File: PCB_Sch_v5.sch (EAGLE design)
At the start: 51 parts, among them IC1 CP2104, M1 C0720B001F, Q1 MMBT2222LT1G, Q2 mmbt2222, Q3 DMG3415U, Q4 mmbt2222, SW1 2-1825027-0, SW2 2-1825027-0, SW3 2-1825027-0, SW4 2-1825027-0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

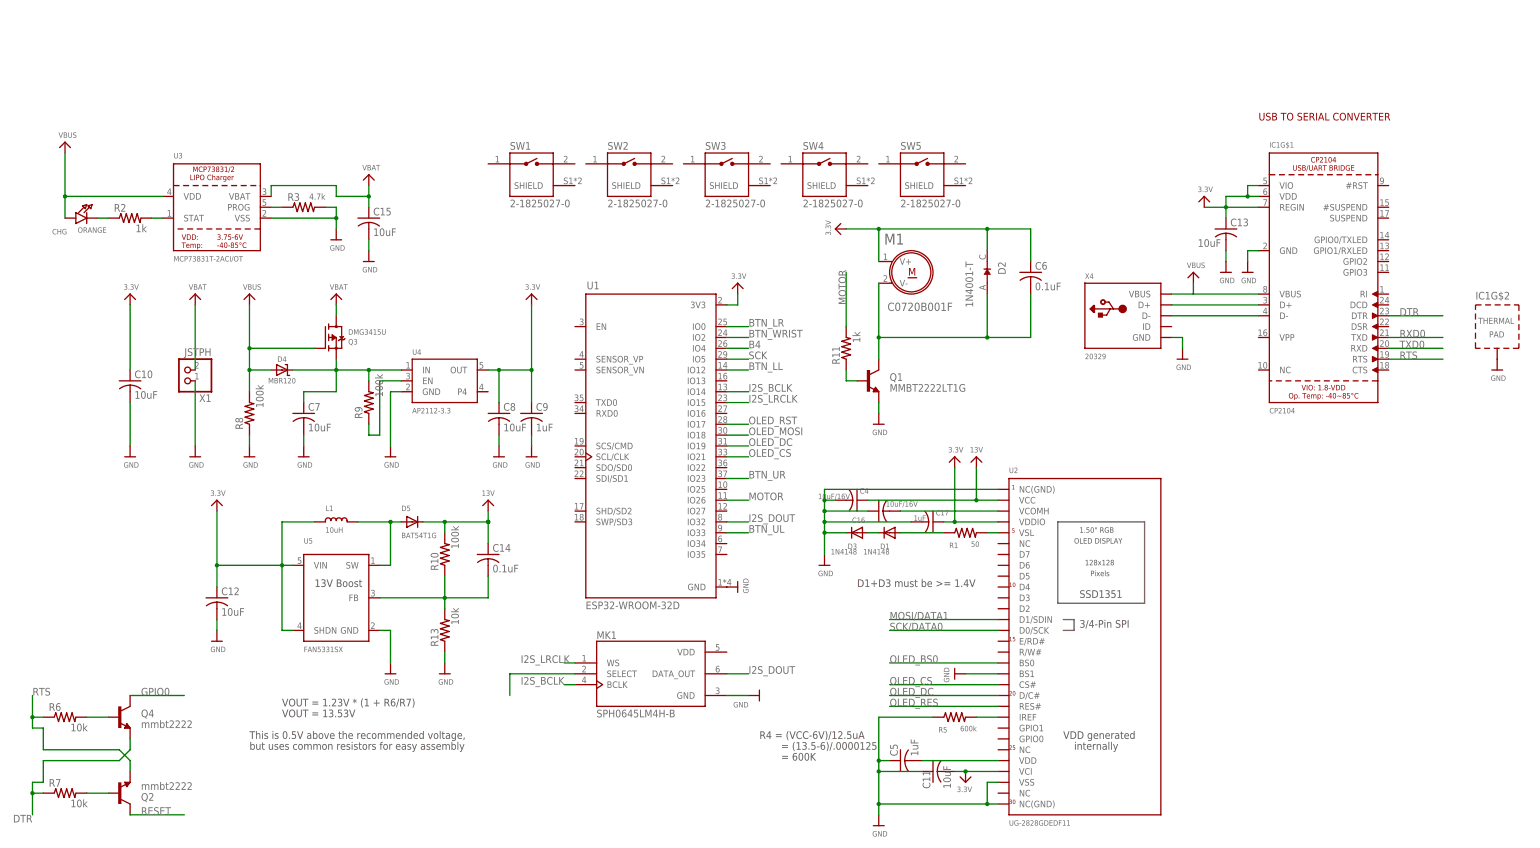
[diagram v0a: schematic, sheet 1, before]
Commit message: Added button to libraries, added debouncing caps
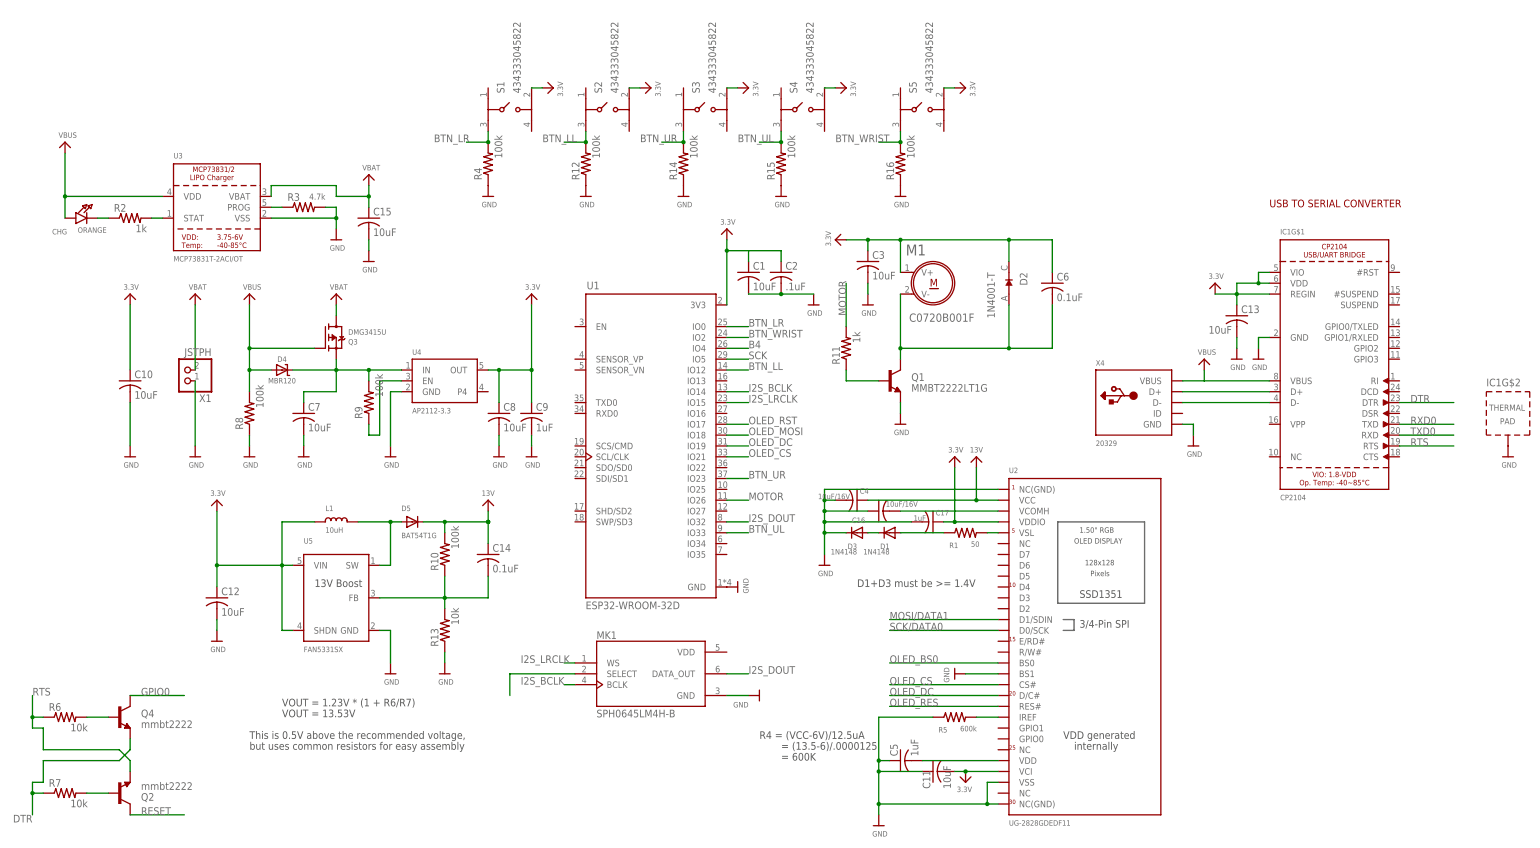
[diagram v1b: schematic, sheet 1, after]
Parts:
- removed SW1, SW2, SW3, SW4, SW5: 2-1825027-0, 2-1825027-0:2-1825027-0
- added C1, C3: 10uF, rcl:C-USC0603
- added C2: .1uF, rcl:C-USC0603
- added R12, R14, R15, R16, R4: 100k, rcl:R-US_R0603
- added S1, S2, S3, S4, S5: 434333045822, 434333045822:434333045822
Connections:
- net 3.3V: now also C1.1, C2.1, C3.1, S1.4, S2.4, S3.4, S4.4, S5.4
- net BTN_LL: now also R12.2, S2.1
- net BTN_LR: now also R4.2, S1.1
- net BTN_UL: now also R15.2, S4.1
- net BTN_UR: now also R14.2, S3.1
- net BTN_WRIST: now also R16.2, S5.1
- net GND: now also C1.2, C2.2, C3.2, R12.1, R14.1, R15.1, R16.1, R4.1
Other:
- moved on the sheet: C13, C6, D2, IC1G$1, IC1G$2, M1, Q1, X4

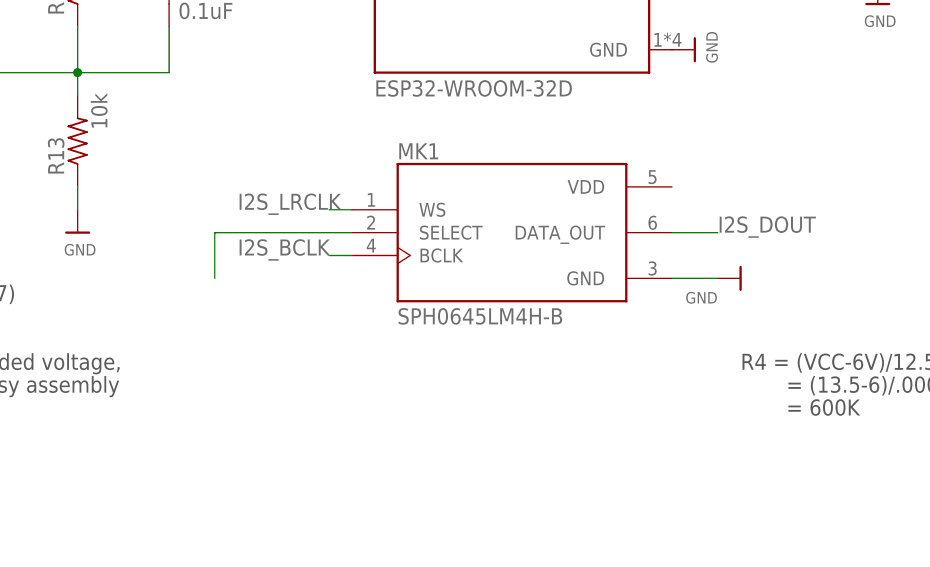
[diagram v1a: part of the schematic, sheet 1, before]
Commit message: added resistor to microphone
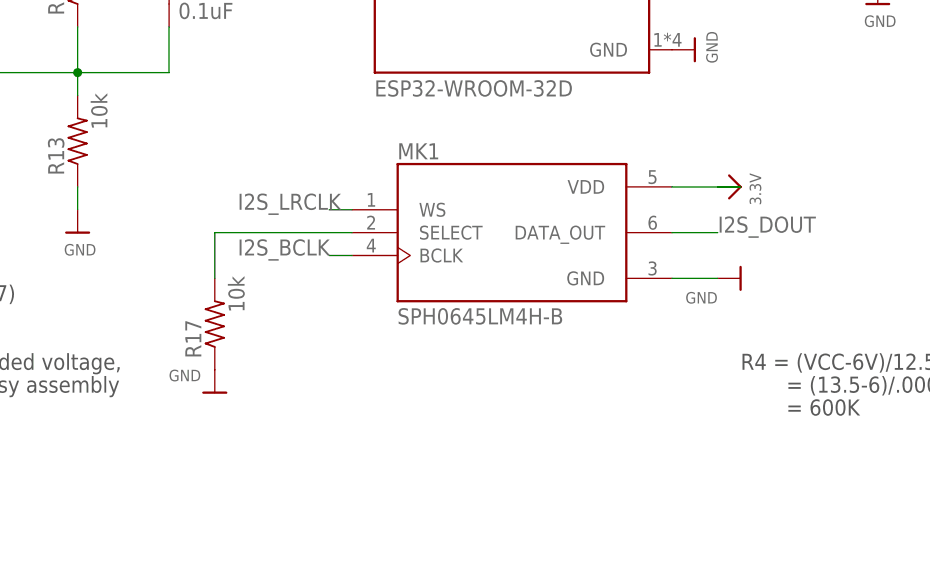
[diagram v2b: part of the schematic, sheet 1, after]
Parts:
- added R17: 10k, rcl:R-US_R0603
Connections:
- new net N$21: MK1.VDD
- net GND: now also R17.1
- net N$4: now also R17.2
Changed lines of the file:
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@@
 <part name="U$49" library="microbuilder" deviceset="3.3V" device=""/>
 <part name="U$50" library="microbuilder" deviceset="3.3V" device=""/>
+<part name="U$51" library="microbuilder" deviceset="3.3V" device=""/>
+<part name="R17" library="rcl" library_urn="urn:adsk.eagle:library:334" deviceset="R-US_" device="R0603" package3d_urn="urn:adsk.eagle:package:23555/2" value="10k"/>
+<part name="U$52" library="microbuilder" deviceset="GND" device=""/>
 </parts>
 <sheets>
@@
 <attribute name="VALUE" x="115.316" y="131.064" size="1.27" layer="96" rot="R270"/>
 </instance>
+<instance part="U$51" gate="G$1" x="66.04" y="-2.54" smashed="yes" rot="R270">
+<attribute name="VALUE" x="67.056" y="-1.016" size="1.27" layer="96" rot="R270"/>
+</instance>
+<instance part="R17" gate="G$1" x="7.62" y="-17.78" smashed="yes" rot="R90">
+<attribute name="NAME" x="6.1214" y="-21.59" size="1.778" layer="95" rot="R90"/>
+<attribute name="VALUE" x="10.922" y="-16.51" size="1.778" layer="96" rot="R90"/>
+</instance>
+<instance part="U$52" gate="G$1" x="7.62" y="-25.4" smashed="yes">
+<attribute name="VALUE" x="6.096" y="-22.86" size="1.27" layer="96" rot="R180"/>
+</instance>
 </instances>
 <busses>
@@
 <pinref part="U$45" gate="G$1" pin="GND"/>
 </segment>
+<segment>
+<pinref part="R17" gate="G$1" pin="1"/>
+<pinref part="U$52" gate="G$1" pin="GND"/>
+</segment>
 </net>
 <net name="MOSI/DATA1" class="0">
@@
 <pinref part="S5" gate="G$1" pin="4"/>
 </segment>
+<segment>
+<pinref part="U$51" gate="G$1" pin="3.3V"/>
+<wire x1="63.5" y1="-2.54" x2="66.04" y2="-2.54" width="0.1524" layer="91"/>
+</segment>
 </net>
 <net name="13V" class="0">
@@
 <wire x1="22.86" y1="-7.62" x2="7.62" y2="-7.62" width="0.1524" layer="91"/>
 <wire x1="7.62" y1="-7.62" x2="7.62" y2="-12.7" width="0.1524" layer="91"/>
-</segment>
-</net>
+<pinref part="R17" gate="G$1" pin="2"/>
+</segment>
+</net>
+<net name="N$21" class="0">
+<segment>
+<pinref part="MK1" gate="G$1" pin="VDD"/>
+<wire x1="58.42" y1="-2.54" x2="66.04" y2="-2.54" width="0.1524" layer="91"/>
+</segment>
+</net>
